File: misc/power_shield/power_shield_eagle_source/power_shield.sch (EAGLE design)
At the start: 29 parts

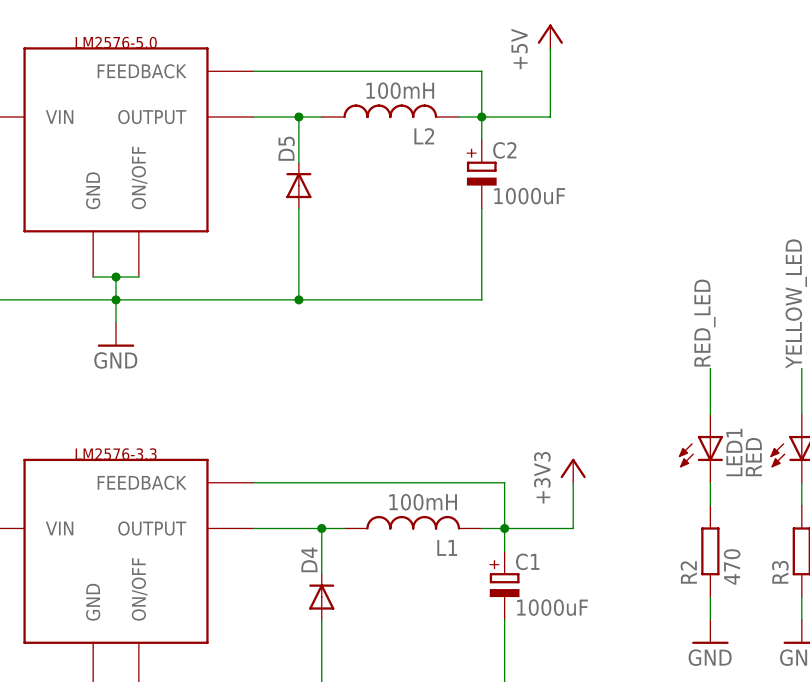
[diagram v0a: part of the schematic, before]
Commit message: Seperated the electronics
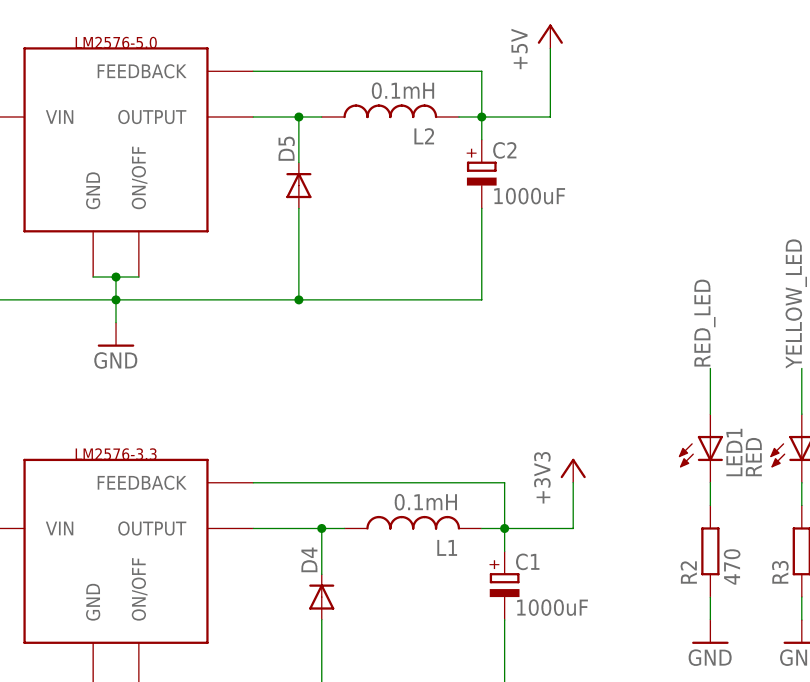
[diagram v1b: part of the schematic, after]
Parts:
- L1, L2: value 100mH -> 0.1mH
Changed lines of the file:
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@@
 <parts>
 <part name="U$1" library="mylib" deviceset="UNO32_SHIELD" device=""/>
-<part name="L1" library="rcl" deviceset="L-US" device="6000-XXX-RC" value="100mH"/>
-<part name="L2" library="rcl" deviceset="L-US" device="6000-XXX-RC" value="100mH"/>
+<part name="L1" library="rcl" deviceset="L-US" device="6000-XXX-RC" value="0.1mH"/>
+<part name="L2" library="rcl" deviceset="L-US" device="6000-XXX-RC" value="0.1mH"/>
 <part name="C1" library="rcl" deviceset="CPOL-EU" device="150CLZ-1010" value="1000uF"/>
 <part name="C2" library="rcl" deviceset="CPOL-EU" device="150CLZ-1010" value="1000uF"/>
